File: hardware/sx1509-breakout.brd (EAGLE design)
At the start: 27.9 x 27.9 mm, 23 parts, among them U1 SX1509

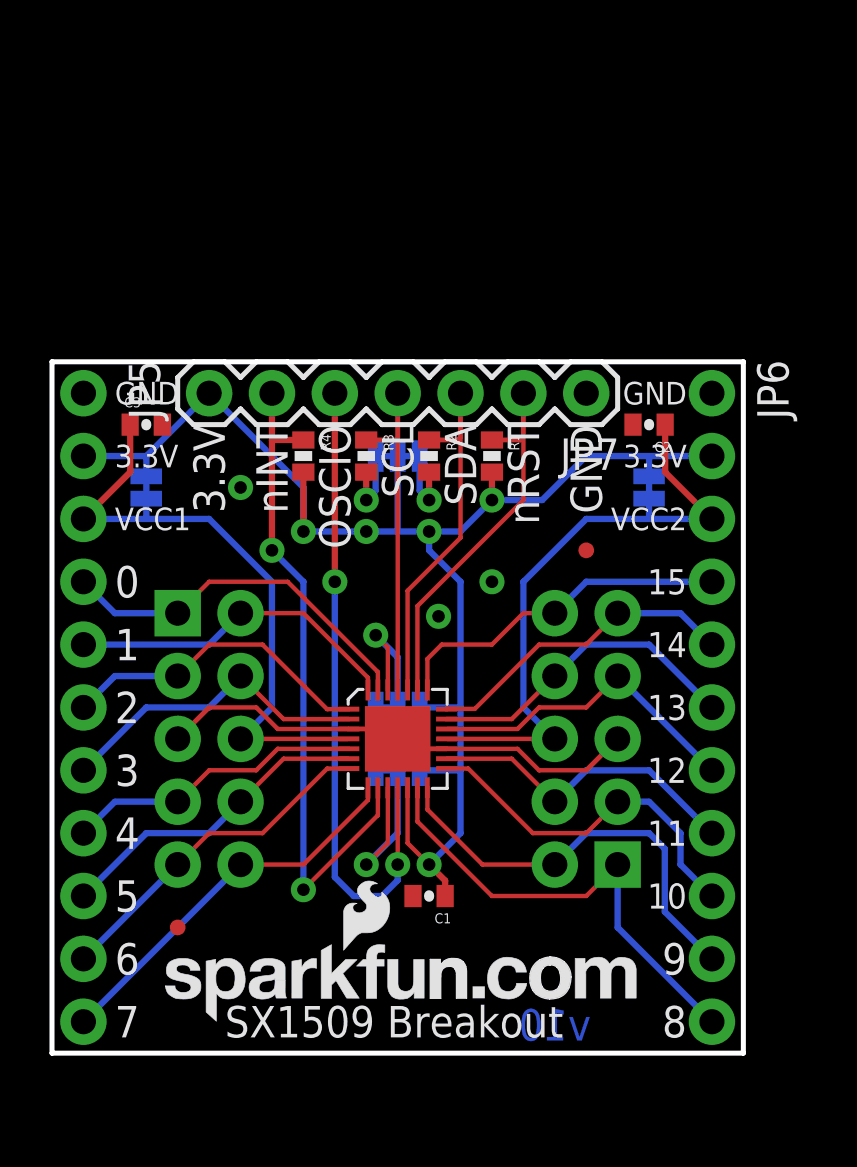
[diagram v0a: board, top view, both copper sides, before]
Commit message: Initial commit of v1.1
- Added standoff holes
- Changed I2C headers to match SparkFun standard
- Added I2C pins to both sides to allow cascading boards.
- Updated Eagle libraries
- Updated 0402 packages to 0603.
- Increase fiducial size
- Updated logos
- Added 10k resistors to SJ2 and SJ3.
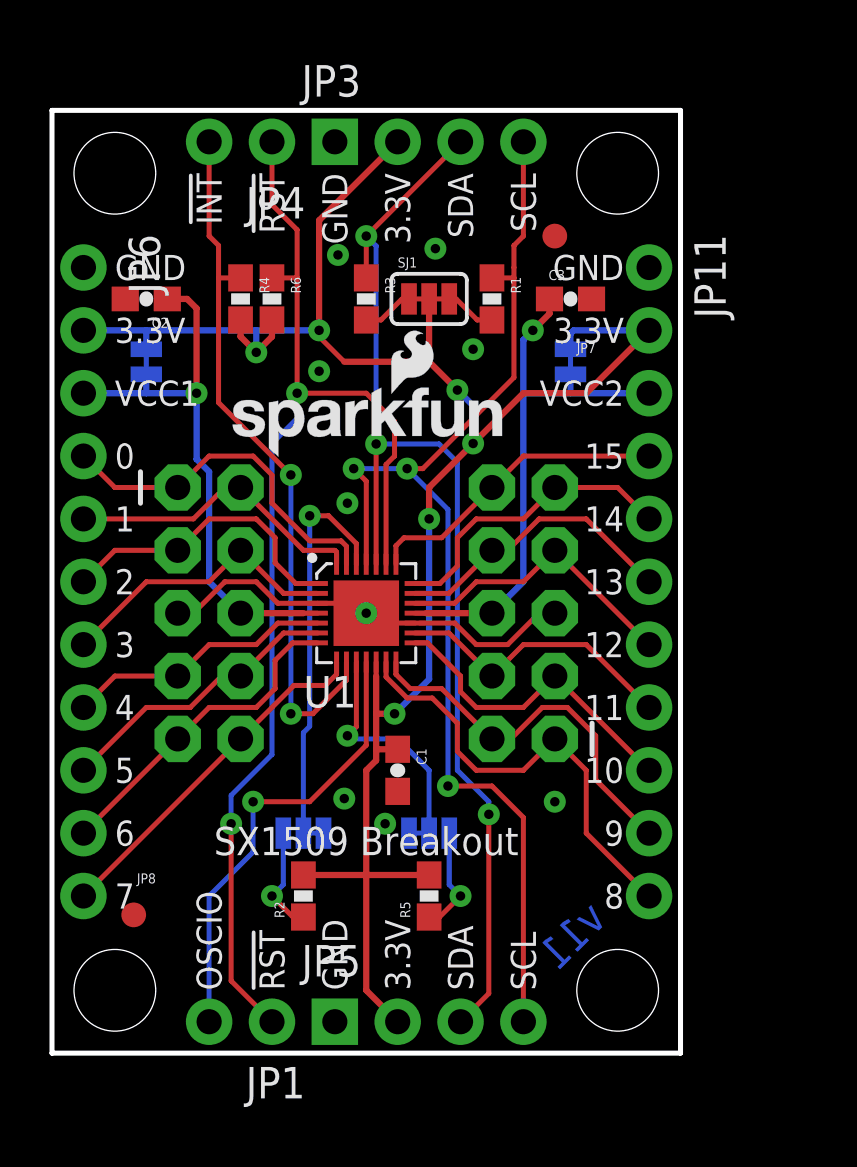
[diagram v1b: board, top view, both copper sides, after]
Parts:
- removed JP2: IDC-5x2, SparkFun-Connectors:2X5-SHROUDED-NO_SILK
- removed U$1: OSHW-LOGOS, SparkFun-Aesthetics:OSHW-LOGO-S
- added FRAME1: (no value), SparkFun-Aesthetics:CREATIVE_COMMONS
- added JP10: FIDUCIAL1X2, SparkFun:FIDUCIAL-1X2
- added JP11: (no value), SparkFun-Connectors:1X11_NO_SILK
- added LOGO1: SFE_LOGO_NAME_FLAME.1_INCH, SparkFun-Aesthetics:SFE_LOGO_NAME_FLAME_.1
- added LOGO2: SFE_LOGO_FLAME.1_INCH, SparkFun-Aesthetics:SFE_LOGO_FLAME_.1
- added LOGO3: OSHW-LOGOS, SparkFun-Aesthetics:OSHW-LOGO-S
- added R5, R6: 10K, SparkFun-Resistors:0603-RES
- added STANDOFF1, STANDOFF2, STANDOFF3, STANDOFF4: STAND-OFF, SparkFun-Electromechanical:STAND-OFF
- C1, C2, C3: device SparkFun-Passives:0402-CAP -> SparkFun-Capacitors:0603-CAP
- JP1: value IDC-5X2 -> (none); device SparkFun-Connectors:2X5-SHROUDED-NO_SILK -> SparkFun-Connectors:1X02_NO_SILK
- JP3: value LOGO-SFENEW -> (none); device SparkFun-Aesthetics:SFE-NEW-WEBLOGO -> SparkFun-Connectors:1X04_NO_SILK
- JP4: value LOGO-SFESK -> (none); device SparkFun-Aesthetics:SFE-LOGO-FLAME -> SparkFun-Connectors:1X02_NO_SILK
- JP5: device SparkFun-Connectors:1X11_NO_SILK -> SparkFun-Connectors:1X04_NO_SILK
- JP7: value (none) -> IDC-5X2; device SparkFun-Connectors:1X07 -> SparkFun-Connectors:2X5-SHROUDED-NS
- JP8: value FIDUCIALUFIDUCIAL -> IDC-5x2; device SparkFun:MICRO-FIDUCIAL -> SparkFun-Connectors:2X5-SHROUDED-NS
- JP9: value FIDUCIALUFIDUCIAL -> FIDUCIAL1X2; device SparkFun:MICRO-FIDUCIAL -> SparkFun:FIDUCIAL-1X2
- R1, R2, R3, R4: value 10k -> 10K; device SparkFun-Passives:0402-RES -> SparkFun-Resistors:0603-RES
- SJ1: device SparkFun-Passives:SJ_3 -> SparkFun-Passives:PAD-JUMPER-3-3OF3_NC_BY_TRACE_YES_SILK_FULL_BOX
- SJ2: device SparkFun-Passives:SJ_3 -> SparkFun-Passives:PAD-JUMPER-3-2OF3_NC_BY_TRACE_YES_SILK_FULL_BOX
- SJ3: device SparkFun-Passives:SJ_2S-NO -> SparkFun-Passives:PAD-JUMPER-3-2OF3_NC_BY_TRACE_YES_SILK_FULL_BOX
- SJ4: device SparkFun-Passives:SJ_2S-NO -> SparkFun-Passives:PAD-JUMPER-2-NC_BY_TRACE_YES_SILK
- SJ5: device SparkFun-Passives:SJ_3 -> SparkFun-Passives:PAD-JUMPER-2-NC_BY_TRACE_YES_SILK
- moved JP3 36.2 mm to (11.4, 36.8)
- moved JP4 35.2 mm to (8.89, 36.8), flipped to the top, turned to 180 degrees
- moved JP9 31.8 mm to (20.3, 33.0)
- moved JP5 27.4 mm to (11.4, 1.27), turned to 0 degrees
- moved JP6 25.9 mm to (1.27, 31.8)
- moved C2 20.9 mm to (3.81, 30.5)
- moved SJ4 20.9 mm to (3.81, 27.9)
- moved SJ1 19.1 mm to (15.2, 30.5), flipped to the top
- moved R2 18.5 mm to (10.2, 6.35), turned to 90 degrees
- moved SJ3 18.1 mm to (15.2, 8.89), turned to 0 degrees
- moved C3 17.9 mm to (21.0, 30.5)
- moved JP1 17.1 mm to (8.89, 1.27)
- moved JP8 15.5 mm to (6.35, 17.8)
- moved JP7 9.25 mm to (19.1, 17.8)
- moved SJ5 7.96 mm to (21.0, 27.9), turned to 90 degrees
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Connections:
- removed net NINT: JP7.6, R4.1, U1.9
- removed net NRESET: JP7.2, R1.1, U1.23
- new net !INT: JP4.2, R4.1, U1.9
- new net !RESET: JP1.1, JP4.1, R6.1, U1.23
- new net N$8: R2.1, SJ2.1
- new net N$9: R5.1, SJ3.1
- net 0: now also JP6.4, JP8.1; no longer JP2.1, JP5.4
- net 1: now also JP6.5, JP8.2; no longer JP2.2, JP5.5
- net 10: now also JP11.9, JP7.3; no longer JP1.3, JP6.9
- net 11: now also JP11.8, JP7.4; no longer JP1.4, JP6.8
- net 12: now also JP11.7, JP7.7; no longer JP1.7, JP6.7
- net 13: now also JP11.6, JP7.8; no longer JP1.8, JP6.6
- net 14: now also JP11.5, JP7.9; no longer JP1.9, JP6.5
- net 15: now also JP11.4, JP7.10; no longer JP1.10, JP6.4
- net 2: now also JP6.6, JP8.3; no longer JP2.3, JP5.6
- net 3: now also JP6.7, JP8.4; no longer JP2.4, JP5.7
- net 3.3V: now also JP11.2, JP3.2, R2.2, R5.2, R6.2, SJ1.2; no longer JP7.7, R1.2, SJ1.1, SJ2.3, SJ3.2
- net 4: now also JP6.8, JP8.7; no longer JP2.7, JP5.8
- net 5: now also JP6.9, JP8.8; no longer JP2.8, JP5.9
- net 6: now also JP6.10, JP8.9; no longer JP2.9, JP5.10
- net 7: now also JP6.11, JP8.10; no longer JP2.10, JP5.11
- net 8: now also JP11.11, JP7.1; no longer JP1.1, JP6.11
- net 9: now also JP11.10, JP7.2; no longer JP1.2, JP6.10
- net ADDR1: now also SJ3.2; no longer SJ1.2
- net GND: now also JP11.1, JP3.1, JP7.5, JP8.5, SJ2.3, SJ3.3; no longer JP1.5, JP2.5, JP7.1, SJ1.3, SJ2.1
- net N$1: now also R1.2, SJ1.3; no longer R3.2, SJ5.3
- net N$2: now also R3.2, SJ1.1; no longer R2.2, SJ5.1
- net OSCIO: now also JP1.2; no longer JP7.5
- net SCL: now also JP3.4, JP5.4, R1.1; no longer JP7.4, R3.1
- net SDA: now also JP3.3, JP5.3, R3.1; no longer JP7.3, R2.1
- net VCC1: now also C2.1, JP6.3, JP8.6, SJ4.1; no longer C3.1, JP2.6, JP5.3, SJ3.1
- net VCC2: now also C3.1, JP11.3, JP7.6, SJ5.1; no longer C2.1, JP1.6, JP6.3, SJ4.1
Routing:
- net !RESET: track 0.00 -> 49.1 mm, vias 0 -> 2
- net SCL: track 13.3 -> 48.0 mm, vias 0 -> 3
- net SDA: track 14.2 -> 47.7 mm, vias 0 -> 3
- net !INT: track 0.00 -> 28.9 mm, vias 0 -> 2
- net NINT: track 27.2 -> 0.00 mm, vias 2 -> 0
- net 3.3V: track 62.1 -> 82.0 mm, vias 5 -> 6
- net NRESET: track 15.1 -> 0.00 mm
- net ADDR0: track 5.71 -> 16.1 mm
- net OSCIO: track 26.4 -> 18.5 mm, vias 2 -> 1
- net N$9: track 0.00 -> 4.35 mm, vias 0 -> 1
- net N$8: track 0.00 -> 4.35 mm, vias 0 -> 1
- net VCC2: track 25.3 -> 22.6 mm, vias 0 -> 1
- net VCC1: track 25.3 -> 22.8 mm, vias 0 -> 1
- net GND: track 19.9 -> 17.8 mm, vias 3 -> 9
- net 9: track 17.4 -> 15.5 mm
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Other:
- board size 27.9 x 27.9 mm -> 25.4 x 38.1 mm
- board text added: "!INT"
- board text added: "!RST"
- board text added: "ADD0"
- board text added: "ADD1"
- board text added: "I2C ADD"
- board text added: "Jim Lindblom"
- board text added: "v11"
- board text removed: "ADDR0"
- board text removed: "ADDR1"
- board text removed: "Breakout"
- board text removed: "C ADDR"
- board text removed: "I"
- board text removed: "SX1509"
- board text removed: "nINT"
- board text removed: "nRST"
- board text removed: "v10"

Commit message: Labeling SJ4 and SJ5.
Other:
- board text added: "SJ4"
- board text added: "SJ5"
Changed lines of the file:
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@@
 <text x="8.001" y="8.89" size="1.016" layer="22" font="vector" ratio="15" rot="MR0" align="center">1</text>
 <text x="52.07" y="-8.89" size="1.27" layer="51" font="vector" ratio="15">Jim Lindblom</text>
+<text x="4.826" y="27.94" size="0.889" layer="22" font="vector" ratio="15" rot="MR0" align="center-right">SJ4</text>
+<text x="19.685" y="27.94" size="0.889" layer="22" font="vector" ratio="15" rot="MR180" align="center-right">SJ5</text>
 </plain>
 <attributes>

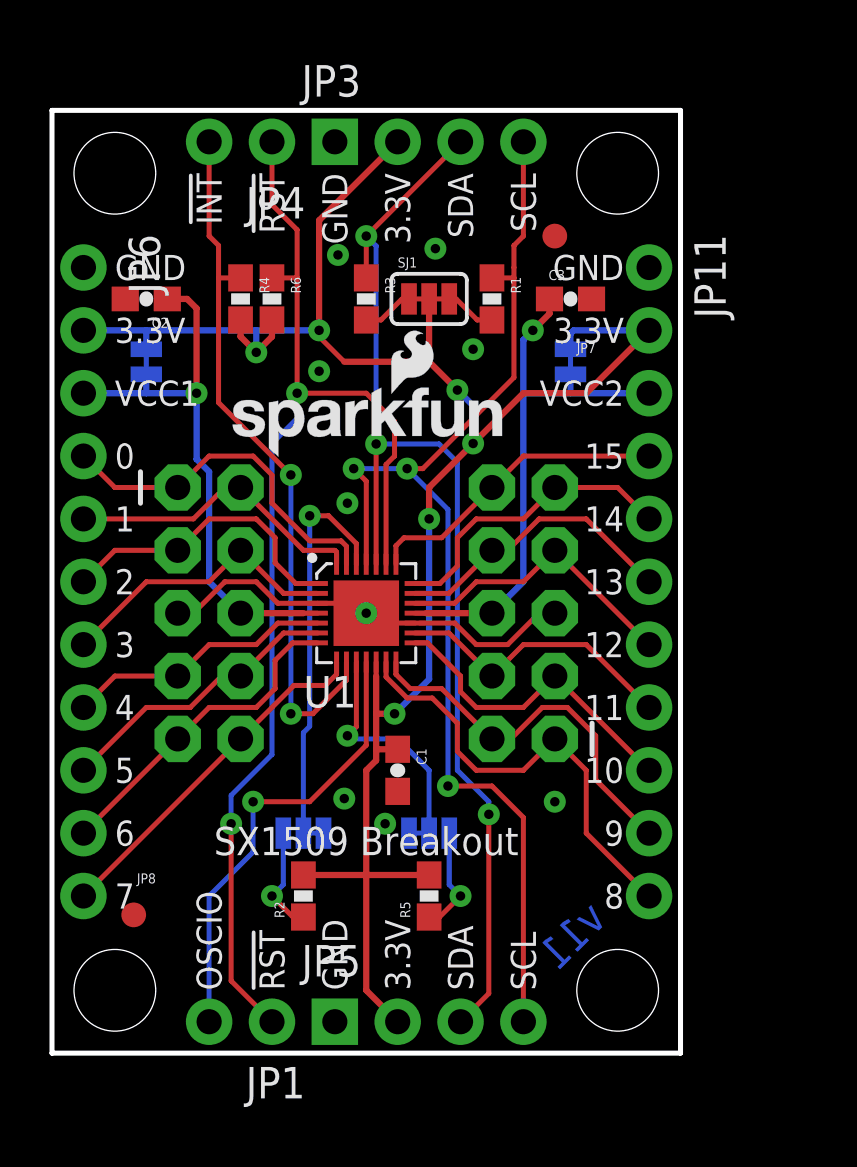
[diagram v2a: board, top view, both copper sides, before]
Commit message: Adding silk around headers. Labeling SJ1.
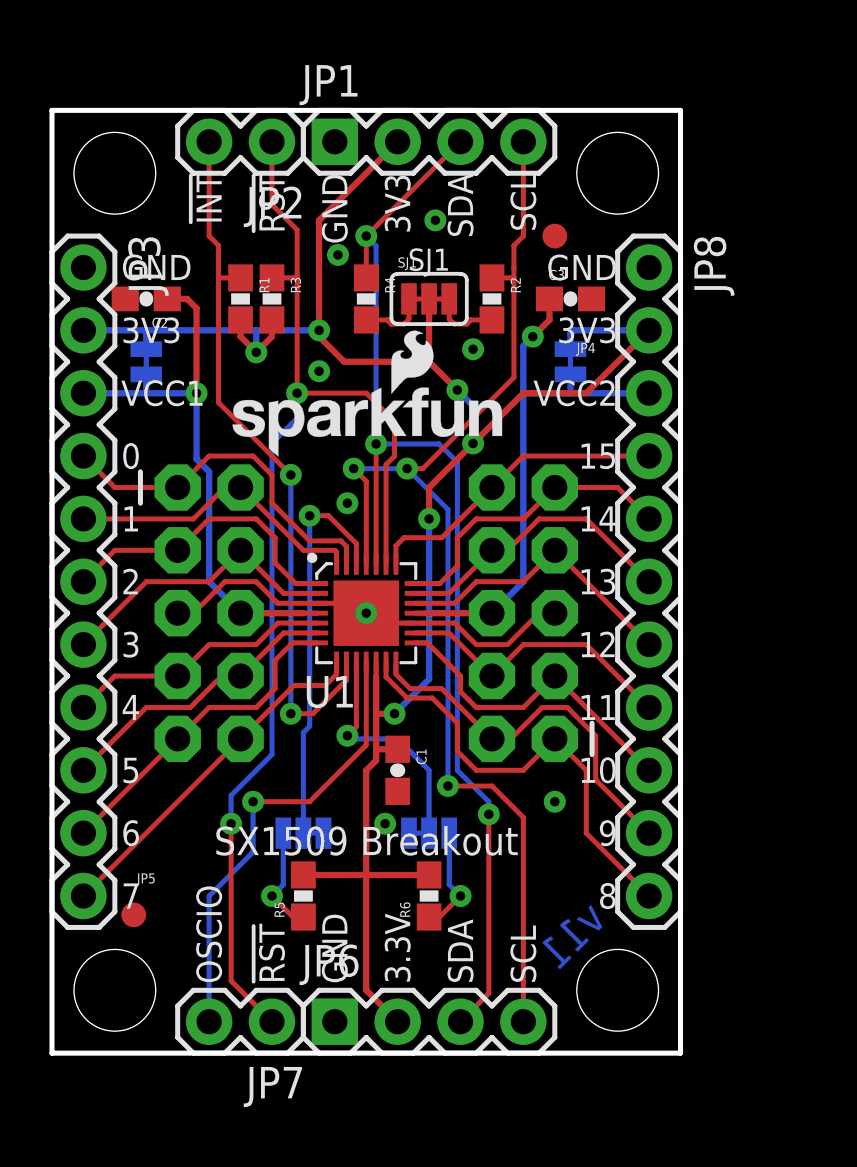
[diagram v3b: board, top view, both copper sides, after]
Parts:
- removed JP11: (no value), SparkFun-Connectors:1X11_NO_SILK
- added JP2: (no value), SparkFun-Connectors:1X02
- JP1: device SparkFun-Connectors:1X02_NO_SILK -> SparkFun-Connectors:1X04
- JP3: device SparkFun-Connectors:1X04_NO_SILK -> SparkFun-Connectors:1X11
- JP4: value (none) -> IDC-5X2; device SparkFun-Connectors:1X02_NO_SILK -> SparkFun-Connectors:2X5-SHROUDED-NS
- JP5: value (none) -> IDC-5x2; device SparkFun-Connectors:1X04_NO_SILK -> SparkFun-Connectors:2X5-SHROUDED-NS
- JP6: device SparkFun-Connectors:1X11_NO_SILK -> SparkFun-Connectors:1X04
- JP7: value IDC-5X2 -> (none); device SparkFun-Connectors:2X5-SHROUDED-NS -> SparkFun-Connectors:1X02
- JP8: value IDC-5x2 -> (none); device SparkFun-Connectors:2X5-SHROUDED-NS -> SparkFun-Connectors:1X11
- SJ2, SJ3: device SparkFun-Passives:PAD-JUMPER-3-2OF3_NC_BY_TRACE_YES_SILK_FULL_BOX -> SparkFun-Passives:PAD-JUMPER-2-NC_BY_TRACE_YES_SILK
- SJ4, SJ5: device SparkFun-Passives:PAD-JUMPER-2-NC_BY_TRACE_YES_SILK -> SparkFun-Passives:PAD-JUMPER-3-2OF3_NC_BY_TRACE_YES_SILK_FULL_BOX
- moved FRAME1 36.8 mm to (-15.5, -8.89)
- moved JP1 35.7 mm to (11.4, 36.8), turned to 0 degrees
- moved JP6 32.1 mm to (11.4, 1.27), turned to 0 degrees
- moved R2 25.3 mm to (17.8, 30.5), turned to 270 degrees
- moved R6 25.0 mm to (15.2, 6.35), turned to 90 degrees
- moved JP8 22.6 mm to (24.1, 31.8), turned to 270 degrees
- moved JP4 21.6 mm to (19.1, 17.8)
- moved SJ2 20.1 mm to (3.81, 27.9), turned to 90 degrees
- moved SJ4 20.1 mm to (10.2, 8.89), turned to 180 degrees
- moved SJ3 19.9 mm to (21.0, 27.9), turned to 90 degrees
- moved SJ5 19.9 mm to (15.2, 8.89), turned to 0 degrees
- moved JP7 19.4 mm to (8.89, 1.27)
- moved JP5 17.3 mm to (6.35, 17.8)
- moved JP3 11.4 mm to (1.27, 31.8), turned to 270 degrees
- moved R1 10.2 mm to (7.62, 30.5)
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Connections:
- net !INT: now also JP2.2, R1.1; no longer JP4.2, R4.1
- net !RESET: now also JP2.1, JP7.1, R3.1; no longer JP1.1, JP4.1, R6.1
- net 0: now also JP3.4, JP5.1; no longer JP6.4, JP8.1
- net 1: now also JP3.5, JP5.2; no longer JP6.5, JP8.2
- net 10: now also JP4.3, JP8.9; no longer JP11.9, JP7.3
- net 11: now also JP4.4, JP8.8; no longer JP11.8, JP7.4
- net 12: now also JP4.7, JP8.7; no longer JP11.7, JP7.7
- net 13: now also JP4.8, JP8.6; no longer JP11.6, JP7.8
- net 14: now also JP4.9, JP8.5; no longer JP11.5, JP7.9
- net 15: now also JP4.10, JP8.4; no longer JP11.4, JP7.10
- net 2: now also JP3.6, JP5.3; no longer JP6.6, JP8.3
- net 3: now also JP3.7, JP5.4; no longer JP6.7, JP8.4
- net 3.3V: now also JP1.2, JP8.2, R1.2, R3.2, SJ2.2, SJ3.2; no longer JP11.2, JP5.2, R2.2, R4.2, SJ4.2, SJ5.2
- net 4: now also JP3.8, JP5.7; no longer JP6.8, JP8.7
- net 5: now also JP3.9, JP5.8; no longer JP6.9, JP8.8
- net 6: now also JP3.10, JP5.9; no longer JP6.10, JP8.9
- net 7: now also JP3.11, JP5.10; no longer JP6.11, JP8.10
- net 8: now also JP4.1, JP8.11; no longer JP11.11, JP7.1
- net 9: now also JP4.2, JP8.10; no longer JP11.10, JP7.2
- net ADDR0: now also SJ4.2; no longer SJ2.2
- net ADDR1: now also SJ5.2; no longer SJ3.2
- net GND: now also JP1.1, JP4.5, JP5.5, JP8.1, SJ4.3, SJ5.3; no longer JP11.1, JP5.1, JP7.5, JP8.5, SJ2.3, SJ3.3
- net N$1: now also R2.2; no longer R1.2
- net N$2: now also R4.2; no longer R3.2
- net N$8: now also R5.1, SJ4.1; no longer R2.1, SJ2.1
- net N$9: now also R6.1, SJ5.1; no longer R5.1, SJ3.1
- net OSCIO: now also JP7.2; no longer JP1.2
- net SCL: now also JP1.4, JP6.4, R2.1; no longer JP3.4, JP5.4, R1.1
- net SDA: now also JP1.3, JP6.3, R4.1; no longer JP3.3, JP5.3, R3.1
- net VCC1: now also JP3.3, JP5.6, SJ2.1; no longer JP6.3, JP8.6, SJ4.1
- net VCC2: now also JP4.6, JP8.3, SJ3.1; no longer JP11.3, JP7.6, SJ5.1
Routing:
- net N$2: track 2.08 -> 2.69 mm
- net N$1: track 2.08 -> 2.69 mm
- net GND: vias 9 -> 8
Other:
- board text added: "3V3"
- board text added: "SJ1"
- board text added: "SJ2"
- board text added: "SJ3"
- board text removed: "SJ4"
- board text removed: "SJ5"
